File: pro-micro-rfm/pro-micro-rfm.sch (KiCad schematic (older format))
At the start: 6 parts

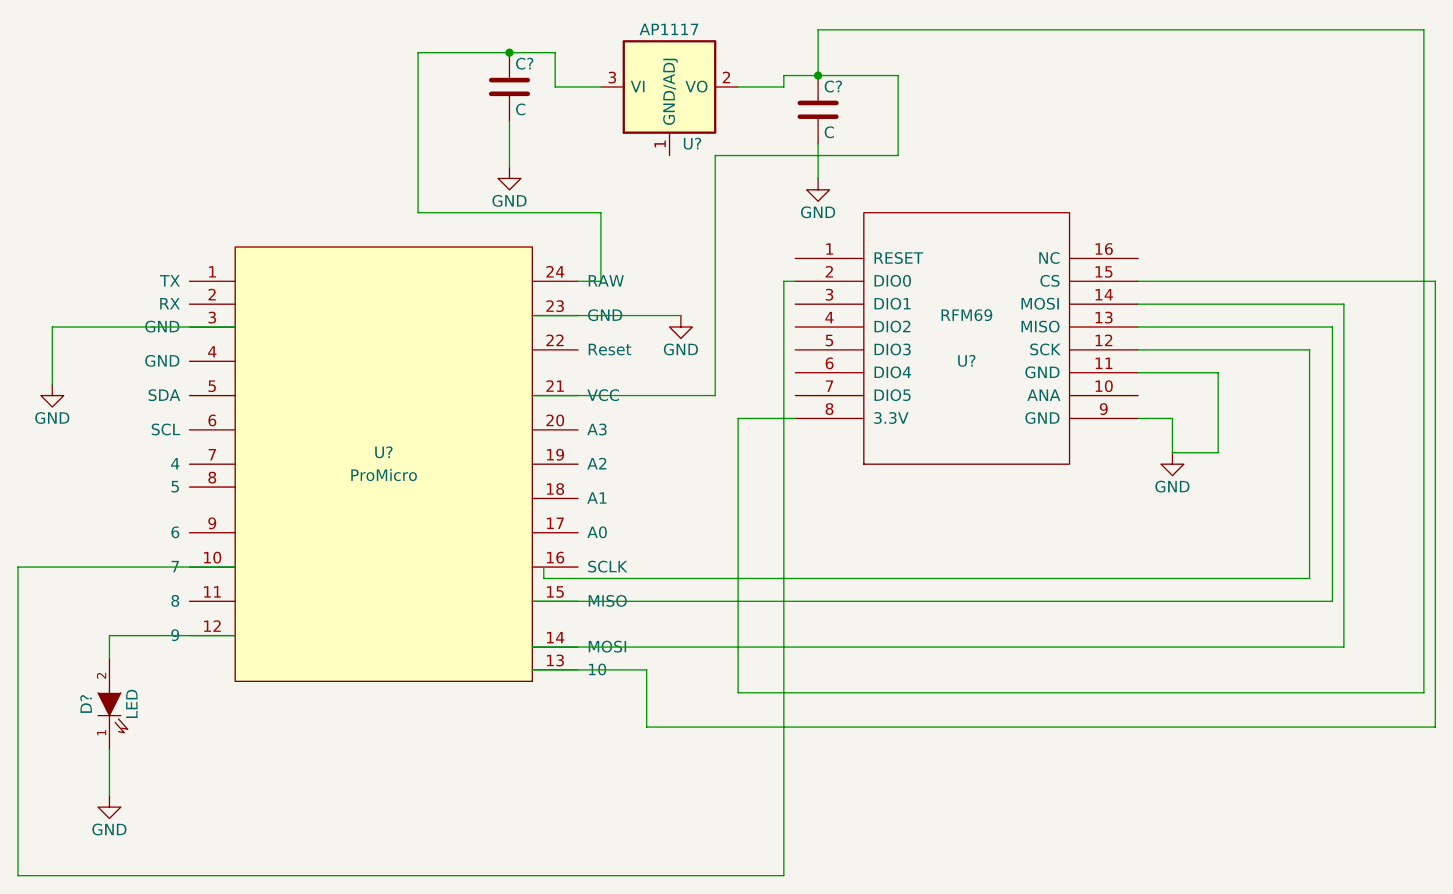
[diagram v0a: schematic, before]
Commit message: minor pcb edits misssed sck line
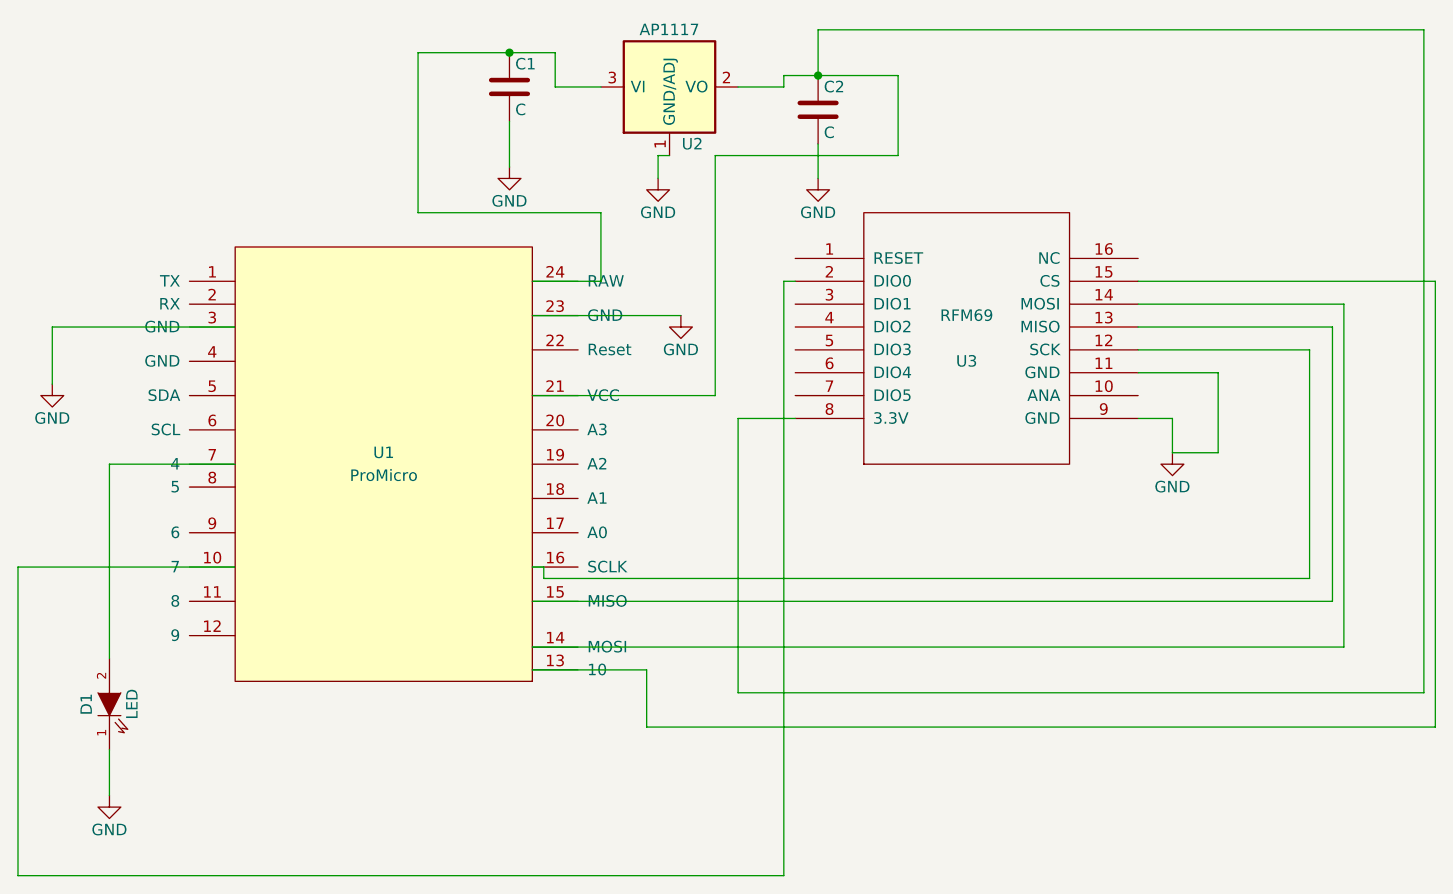
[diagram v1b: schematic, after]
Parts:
- C1, C2: renamed from C?; footprint (none) -> Capacitors_SMD:C_0805
- D1: renamed from D?; footprint (none) -> LEDs:LED-0805
- U1: renamed from U?; footprint (none) -> pro-micro:ARDUINO_PRO_MINI
- U2: renamed from U?; footprint (none) -> SOT223:SOT223
- U3: renamed from U?; footprint MODULE -> RFM69BreakoutBoardFootPrints:RFM69HW
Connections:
- wire segments 53 -> 56
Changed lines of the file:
@@
 $EndDescr
 $Comp
-L RFM69 U?
+L RFM69 U3
 U 1 1 5589EEAB
 P 5400 2150
-F 0 "U?" H 5400 2050 50  0000 C CNN
+F 0 "U3" H 5400 2050 50  0000 C CNN
 F 1 "RFM69" H 5400 2250 50  0000 C CNN
-F 2 "MODULE" H 5400 1750 50  0001 C CNN
+F 2 "RFM69BreakoutBoardFootPrints:RFM69HW" H 5400 1750 50  0001 C CNN
 F 3 "DOCUMENTATION" H 5450 1650 50  0001 C CNN
 	1    5400 2150
@@
 $EndComp
 $Comp
-L AP1117 U?
+L AP1117 U2
 U 1 1 5589EF2A
 P 4100 1050
-F 0 "U?" H 4200 800 50  0000 C CNN
+F 0 "U2" H 4200 800 50  0000 C CNN
 F 1 "AP1117" H 4100 1300 50  0000 C CNN
-F 2 "" H 4100 1050 60  0000 C CNN
+F 2 "SOT223:SOT223" H 4100 1050 60  0001 C CNN
 F 3 "" H 4100 1050 60  0000 C CNN
 	1    4100 1050
@@
 $EndComp
 $Comp
-L C C?
+L C C1
 U 1 1 5589EF5A
 P 3400 1050
-F 0 "C?" H 3425 1150 50  0000 L CNN
+F 0 "C1" H 3425 1150 50  0000 L CNN
 F 1 "C" H 3425 950 50  0000 L CNN
-F 2 "" H 3438 900 30  0000 C CNN
+F 2 "Capacitors_SMD:C_0805" H 3438 900 30  0001 C CNN
 F 3 "" H 3400 1050 60  0000 C CNN
 	1    3400 1050
@@
 $EndComp
 $Comp
-L C C?
+L C C2
 U 1 1 5589EF87
 P 4750 1150
-F 0 "C?" H 4775 1250 50  0000 L CNN
+F 0 "C2" H 4775 1250 50  0000 L CNN
 F 1 "C" H 4775 1050 50  0000 L CNN
-F 2 "" H 4788 1000 30  0000 C CNN
+F 2 "Capacitors_SMD:C_0805" H 4788 1000 30  0001 C CNN
 F 3 "" H 4750 1150 60  0000 C CNN
 	1    4750 1150
@@
 $EndComp
 $Comp
-L ProMicro U?
+L ProMicro U1
 U 1 1 5589F4B6
 P 2850 2700
-F 0 "U?" H 2850 2750 50  0000 C CNN
+F 0 "U1" H 2850 2750 50  0000 C CNN
 F 1 "ProMicro" H 2850 2650 50  0000 C CNN
-F 2 "" H 2850 2700 60  0000 C CNN
+F 2 "pro-micro:ARDUINO_PRO_MINI" H 2850 2700 60  0001 C CNN
 F 3 "" H 2850 2700 60  0000 C CNN
 	1    2850 2700
@@
 $EndComp
 $Comp
-L GND #PWR?
+L GND #PWR01
 U 1 1 5589F564
 P 3400 1400
-F 0 "#PWR?" H 3400 1150 50  0001 C CNN
+F 0 "#PWR01" H 3400 1150 50  0001 C CNN
 F 1 "GND" H 3400 1250 50  0000 C CNN
 F 2 "" H 3400 1400 60  0000 C CNN
@@
 $EndComp
 $Comp
-L GND #PWR?
+L GND #PWR02
 U 1 1 5589F57D
 P 4750 1450
-F 0 "#PWR?" H 4750 1200 50  0001 C CNN
+F 0 "#PWR02" H 4750 1200 50  0001 C CNN
 F 1 "GND" H 4750 1300 50  0000 C CNN
 F 2 "" H 4750 1450 60  0000 C CNN
@@
 $EndComp
 $Comp
-L GND #PWR?
+L GND #PWR03
 U 1 1 5589F5D5
 P 1400 2350
-F 0 "#PWR?" H 1400 2100 50  0001 C CNN
+F 0 "#PWR03" H 1400 2100 50  0001 C CNN
 F 1 "GND" H 1400 2200 50  0000 C CNN
 F 2 "" H 1400 2350 60  0000 C CNN
@@
 $EndComp
 $Comp
-L GND #PWR?
+L GND #PWR04
 U 1 1 5589F64E
 P 4150 2050
-F 0 "#PWR?" H 4150 1800 50  0001 C CNN
+F 0 "#PWR04" H 4150 1800 50  0001 C CNN
 F 1 "GND" H 4150 1900 50  0000 C CNN
 F 2 "" H 4150 2050 60  0000 C CNN
@@
 $EndComp
 $Comp
-L GND #PWR?
+L GND #PWR05
 U 1 1 5589F68B
 P 6300 2650
-F 0 "#PWR?" H 6300 2400 50  0001 C CNN
+F 0 "#PWR05" H 6300 2400 50  0001 C CNN
 F 1 "GND" H 6300 2500 50  0000 C CNN
 F 2 "" H 6300 2650 60  0000 C CNN
@@
 $EndComp
 $Comp
-L LED D?
+L LED D1
 U 1 1 5589F6D9
 P 1650 3750
-F 0 "D?" H 1650 3850 50  0000 C CNN
+F 0 "D1" H 1650 3850 50  0000 C CNN
 F 1 "LED" H 1650 3650 50  0000 C CNN
-F 2 "" H 1650 3750 60  0000 C CNN
+F 2 "LEDs:LED-0805" H 1650 3750 60  0001 C CNN
 F 3 "" H 1650 3750 60  0000 C CNN
 	1    1650 3750
@@
 $EndComp
 $Comp
-L GND #PWR?
+L GND #PWR06
 U 1 1 5589F772
 P 1650 4150
-F 0 "#PWR?" H 1650 3900 50  0001 C CNN
+F 0 "#PWR06" H 1650 3900 50  0001 C CNN
 F 1 "GND" H 1650 4000 50  0000 C CNN
 F 2 "" H 1650 4150 60  0000 C CNN
@@
 	4750 1300 4750 1450
 Wire Wire Line
-	3700 1900 3800 1900
+	3500 1900 3800 1900
 Wire Wire Line
 	3800 1900 3800 1600
@@
 	6500 2650 6300 2650
 Wire Wire Line
-	2200 3450 1650 3450
-Wire Wire Line
-	1650 3450 1650 3550
-Wire Wire Line
 	1650 4150 1650 3950
 Wire Wire Line
@@
 Wire Wire Line
 	7450 1900 6150 1900
+$Comp
+L GND #PWR07
+U 1 1 558A0986
+P 4050 1450
+F 0 "#PWR07" H 4050 1200 50  0001 C CNN
+F 1 "GND" H 4050 1300 50  0000 C CNN
+F 2 "" H 4050 1450 60  0000 C CNN
+F 3 "" H 4050 1450 60  0000 C CNN
+	1    4050 1450
+	1    0    0    -1
+$EndComp
+Wire Wire Line
+	4050 1450 4050 1350
+Wire Wire Line
+	4050 1350 4100 1350
+Wire Wire Line
+	2200 2700 1650 2700
+Wire Wire Line
+	1650 2700 1650 3550
+Wire Wire Line
+	3550 3150 3500 3150
 $EndSCHEMATC
